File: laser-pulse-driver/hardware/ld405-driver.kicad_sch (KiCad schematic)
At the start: 145 parts, among them J1 9V DC IN, J2 TTL IN, J3 SET MON, J4 I MON, J5 LD OUT, J6 INTERLOCK, K1 G6K-2F-Y 5V, Q1 AO3401A, Q10 AO3400A, Q11 AO3401A, Q2 IRFR9024N, Q3 2N7002, Q4 2N7002, Q5 2N7002, Q6 AO3401A, Q7 AO3401A, Q8 2N7002, Q9 2N7002, SW1 ENABLE, U1 L78M05ABDT, U10 TLV9062, U11 LM2901, U12 74HC14, U13 74HC132, U14 74AHCT1G14, U2 REF3030, U3 TLV9062, U4 TLV9062, U5 SN74LVC1G3157, U7 OPA2192, U8 INA180A1

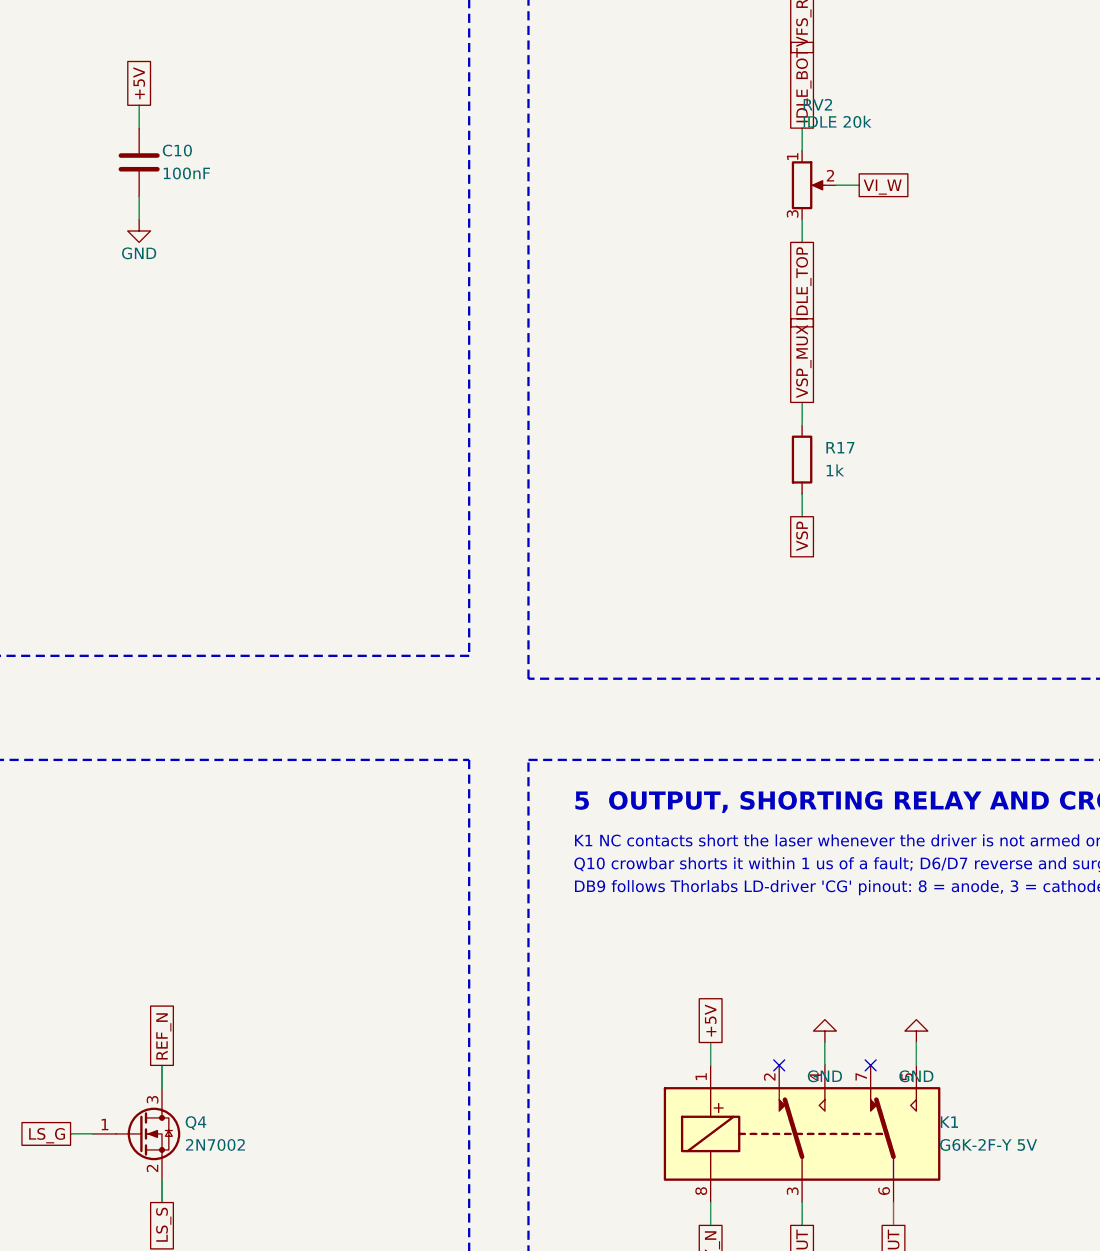
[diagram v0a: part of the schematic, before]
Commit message: laser-pulse-driver: fix relay contacts, toggle holes, REF3030 bypass
Datasheet review:
- K1 (Omron G6K-2F-Y): the normally-closed contacts are 2 and 7, not 4
  and 5. The output short-to-ground was inverted (open when disarmed,
  shorting the diode when armed). GND now goes to pins 2 and 7.
- SW1 (Dailywell 1MS1T2B4M7QES): 0.76 x 1.22 mm tab terminals need the
  datasheet's 1.85 mm holes; the footprint had 1.2 mm.
- C10 1 uF: REF30xx asks for >= 0.47 uF on its supply pin.
- Side-view LED silkscreen marks the cathode end, as is conventional.

Co-Authored-By: Claude Opus 5.5 <noreply@anthropic.com>
Claude-Session: https://claude.ai/code/session_019RAi5HuganNifeSzFvLjAT
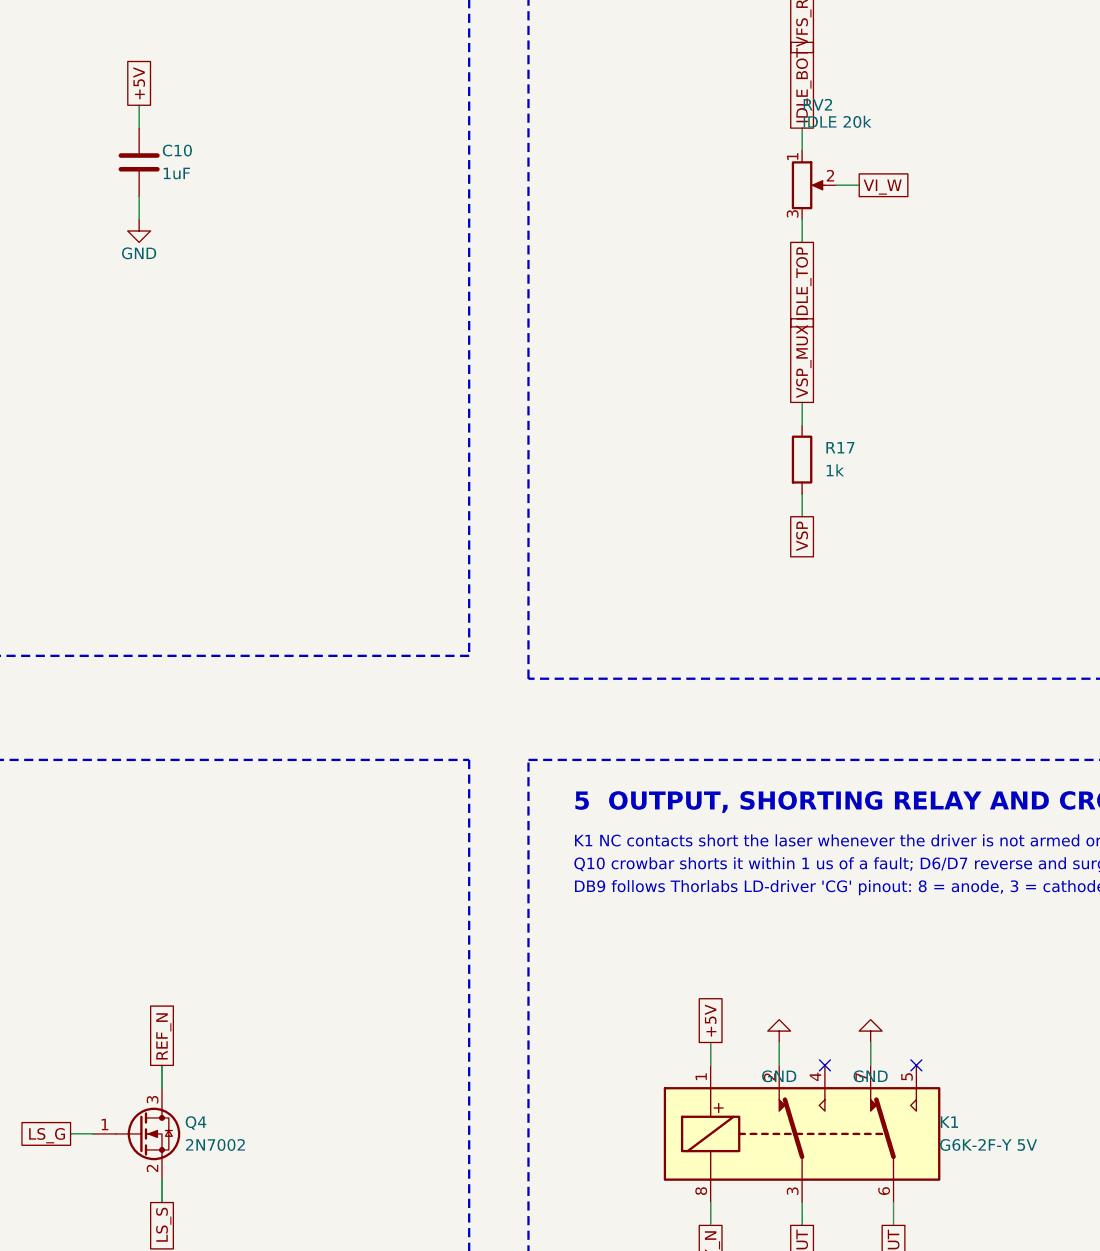
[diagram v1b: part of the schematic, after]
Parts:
- C10: value 100nF -> 1uF; LCSC C14663 -> C15849; MPN CC0603KRX7R9BB104 -> CL10A105KB8NNNC
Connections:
- net GND: now also K1.2, K1.7; no longer K1.4, K1.5
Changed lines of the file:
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@@
 			)
 		)
-		(property "Value" "100nF"
+		(property "Value" "1uF"
 			(at 313.69 116.84 0)
 			(effects
@@
 			)
 		)
-		(property "LCSC" "C14663"
+		(property "LCSC" "C15849"
 			(at 311.15 115.57 0)
 			(effects
@@
 			)
 		)
-		(property "MPN" "CC0603KRX7R9BB104"
+		(property "MPN" "CL10A105KB8NNNC"
 			(at 311.15 115.57 0)
 			(effects
@@
 		)
 	)
-	(no_connect
-		(at 382.27 215.9)
-	)
 	(wire
 		(pts
-			(xy 384.81 231.14)
-			(xy 384.81 233.68)
-		)
-		(stroke
-			(width 0)
-			(type default)
-		)
-	)
-	(global_label "LD_OUT"
-		(shape passive)
-		(at 384.81 233.68 270)
-		(fields_autoplaced yes)
-		(effects
-			(font
-				(size 1.27 1.27)
-			)
-			(justify right)
-		)
-		(property "Intersheetrefs" "${INTERSHEET_REFS}"
-			(at 384.81 233.68 0)
-			(effects
-				(font
-					(size 1.27 1.27)
-				)
-				(hide yes)
-			)
-		)
-	)
-	(wire
-		(pts
-			(xy 387.35 215.9)
-			(xy 387.35 213.36)
+			(xy 382.27 215.9)
+			(xy 382.27 213.36)
 		)
 		(stroke
@@
 	(symbol
 		(lib_id "power:GND")
-		(at 387.35 213.36 180)
+		(at 382.27 213.36 180)
 		(unit 1)
 		(exclude_from_sim no)
@@
 		(fields_autoplaced yes)
 		(property "Reference" "#PWR042"
-			(at 387.35 219.36 0)
+			(at 382.27 219.36 0)
 			(effects
 				(font
@@
 		)
 		(property "Value" "GND"
-			(at 387.35 217.16 0)
+			(at 382.27 217.16 0)
 			(effects
 				(font
@@
 		)
 		(property "Footprint" ""
-			(at 387.35 213.36 0)
+			(at 382.27 213.36 0)
 			(effects
 				(font
@@
 		)
 		(property "Datasheet" ""
-			(at 387.35 213.36 0)
+			(at 382.27 213.36 0)
 			(effects
 				(font
@@
 		)
 		(property "Description" ""
-			(at 387.35 213.36 0)
+			(at 382.27 213.36 0)
 			(effects
 				(font
@@
 		)
 	)
-	(no_connect
-		(at 392.43 215.9)
-	)
 	(wire
 		(pts
-			(xy 394.97 231.14)
-			(xy 394.97 233.68)
+			(xy 384.81 231.14)
+			(xy 384.81 233.68)
 		)
 		(stroke
@@
 	(global_label "LD_OUT"
 		(shape passive)
-		(at 394.97 233.68 270)
+		(at 384.81 233.68 270)
 		(fields_autoplaced yes)
 		(effects
@@
 		)
 		(property "Intersheetrefs" "${INTERSHEET_REFS}"
-			(at 394.97 233.68 0)
+			(at 384.81 233.68 0)
 			(effects
 				(font
@@
 		)
 	)
+	(no_connect
+		(at 387.35 215.9)
+	)
 	(wire
 		(pts
-			(xy 397.51 215.9)
-			(xy 397.51 213.36)
+			(xy 392.43 215.9)
+			(xy 392.43 213.36)
 		)
 		(stroke
@@
 	(symbol
 		(lib_id "power:GND")
-		(at 397.51 213.36 180)
+		(at 392.43 213.36 180)
 		(unit 1)
 		(exclude_from_sim no)
@@
 		(fields_autoplaced yes)
 		(property "Reference" "#PWR043"
-			(at 397.51 219.36 0)
+			(at 392.43 219.36 0)
 			(effects
 				(font
@@
 		)
 		(property "Value" "GND"
-			(at 397.51 217.16 0)
+			(at 392.43 217.16 0)
 			(effects
 				(font
@@
 		)
 		(property "Footprint" ""
-			(at 397.51 213.36 0)
+			(at 392.43 213.36 0)
 			(effects
 				(font
@@
 		)
 		(property "Datasheet" ""
-			(at 397.51 213.36 0)
+			(at 392.43 213.36 0)
 			(effects
 				(font
@@
 		)
 		(property "Description" ""
-			(at 397.51 213.36 0)
+			(at 392.43 213.36 0)
 			(effects
 				(font
@@
 		)
 	)
+	(wire
+		(pts
+			(xy 394.97 231.14)
+			(xy 394.97 233.68)
+		)
+		(stroke
+			(width 0)
+			(type default)
+		)
+	)
+	(global_label "LD_OUT"
+		(shape passive)
+		(at 394.97 233.68 270)
+		(fields_autoplaced yes)
+		(effects
+			(font
+				(size 1.27 1.27)
+			)
+			(justify right)
+		)
+		(property "Intersheetrefs" "${INTERSHEET_REFS}"
+			(at 394.97 233.68 0)
+			(effects
+				(font
+					(size 1.27 1.27)
+				)
+				(hide yes)
+			)
+		)
+	)
+	(no_connect
+		(at 397.51 215.9)
+	)
 	(symbol

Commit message: laser-pulse-driver: review round 2 - Lite-On LEDs, DC jack height, toggle hole
From the review of the design-review page:
- A7: the XINGLIGHT XL-3210 datasheet contradicts itself on the cathode end
  (tape vs outline drawing). The four panel LEDs are now Lite-On LTST-S220
  (TGKT, KSKT, TBKT, KRKT), whose package and tape drawings both label the
  cathode; new footprint to Lite-On's land pattern, same polarity.
- C4: the DC-005 plug axis is 7.0 mm above the board (4.00 below the top of
  the 11 mm body), not 6.5; the rear-panel hole is moved onto it.
- C2: the toggle bushing height was never given by the drawing (6.46 is the
  lever length); measured ~6.45 mm, and the panel hole is widened to
  Ø7.4. The toggle model now has the real terminal shapes and the lever.
- A4: footprint renders put each net label beside its own pad.
- Review sections are labelled and show nuts, washers and typical mating
  plugs; regenerated board (DRC/ERC clean), fab outputs and STLs.

Co-Authored-By: Claude Opus 5.5 <noreply@anthropic.com>
Claude-Session: https://claude.ai/code/session_019RAi5HuganNifeSzFvLjAT
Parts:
- D12: footprint ld405:LED_SideView_XL-3210 -> ld405:LED_SideView_LiteOn_LTST-S220; LCSC C965874 -> C284935; MPN XL-3210SURC -> LTST-S220KRKT
- D16: footprint ld405:LED_SideView_XL-3210 -> ld405:LED_SideView_LiteOn_LTST-S220; LCSC C965876 -> C160468; MPN XL-3210UYC -> LTST-S220KSKT
- D3: footprint ld405:LED_SideView_XL-3210 -> ld405:LED_SideView_LiteOn_LTST-S220; LCSC C965877 -> C160470; MPN XL-3210UGC -> LTST-S220TGKT
- D8: footprint ld405:LED_SideView_XL-3210 -> ld405:LED_SideView_LiteOn_LTST-S220; LCSC C965879 -> C160471; MPN XL-3210UBC -> LTST-S220TBKT
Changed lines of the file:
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@@
 			)
 		)
-		(property "Footprint" "ld405:LED_SideView_XL-3210"
+		(property "Footprint" "ld405:LED_SideView_LiteOn_LTST-S220"
 			(at 770.89 402.59 0)
 			(effects
@@
 			)
 		)
-		(property "LCSC" "C965877"
+		(property "LCSC" "C160470"
 			(at 770.89 402.59 0)
 			(effects
@@
 			)
 		)
-		(property "MPN" "XL-3210UGC"
+		(property "MPN" "LTST-S220TGKT"
 			(at 770.89 402.59 0)
 			(effects
@@
 			)
 		)
-		(property "Footprint" "ld405:LED_SideView_XL-3210"
+		(property "Footprint" "ld405:LED_SideView_LiteOn_LTST-S220"
 			(at 875.03 402.59 0)
 			(effects
@@
 			)
 		)
-		(property "LCSC" "C965874"
+		(property "LCSC" "C284935"
 			(at 875.03 402.59 0)
 			(effects
@@
 			)
 		)
-		(property "MPN" "XL-3210SURC"
+		(property "MPN" "LTST-S220KRKT"
 			(at 875.03 402.59 0)
 			(effects
@@
 			)
 		)
-		(property "Footprint" "ld405:LED_SideView_XL-3210"
+		(property "Footprint" "ld405:LED_SideView_LiteOn_LTST-S220"
 			(at 770.89 433.07 0)
 			(effects
@@
 			)
 		)
-		(property "LCSC" "C965876"
+		(property "LCSC" "C160468"
 			(at 770.89 433.07 0)
 			(effects
@@
 			)
 		)
-		(property "MPN" "XL-3210UYC"
+		(property "MPN" "LTST-S220KSKT"
 			(at 770.89 433.07 0)
 			(effects
@@
 			)
 		)
-		(property "Footprint" "ld405:LED_SideView_XL-3210"
+		(property "Footprint" "ld405:LED_SideView_LiteOn_LTST-S220"
 			(at 875.03 433.07 0)
 			(effects
@@
 			)
 		)
-		(property "LCSC" "C965879"
+		(property "LCSC" "C160471"
 			(at 875.03 433.07 0)
 			(effects
@@
 			)
 		)
-		(property "MPN" "XL-3210UBC"
+		(property "MPN" "LTST-S220TBKT"
 			(at 875.03 433.07 0)
 			(effects
